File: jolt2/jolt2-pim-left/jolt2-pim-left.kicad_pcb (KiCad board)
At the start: 2 copper layers, 151 x 98 mm, 63 parts, among them J1 Conn_01x02_Pin, J10 Conn_01x02_Pin, J11 Conn_01x02_Pin, J12 Conn_01x02_Pin, J13 Conn_01x02_Pin, J14 Conn_01x02_Pin, J15 Conn_01x02_Pin, J16 Conn_01x02_Pin, J17 Conn_01x02_Pin, J18 Conn_01x02_Pin, J19 Conn_01x02_Pin, J2 Conn_01x02_Pin, J20 Conn_01x02_Pin, J21 Conn_01x02_Pin, J22 Conn_01x02_Pin, J23 Conn_01x02_Pin, J24 Conn_01x02_Pin, J25 Conn_01x02_Pin, J26 Conn_01x02_Pin, J27 Conn_01x02_Pin, J28 Conn_01x02_Pin, J29 USB_C_Receptacle_USB2.0_14P, J3 Conn_01x02_Pin, J30 Conn_ARM_JTAG_SWD_10, J31 RJ45, J4 Conn_01x02_Pin, J5 Conn_01x02_Pin, J6 Conn_01x02_Pin, J7 Conn_01x02_Pin, J8 Conn_01x02_Pin, J9 Conn_01x02_Pin, SW1 SW_SPST, SW2 SW_SPST, U1 RP2040, U3 W25Q128JVP, Y1 ABM8-272-T3

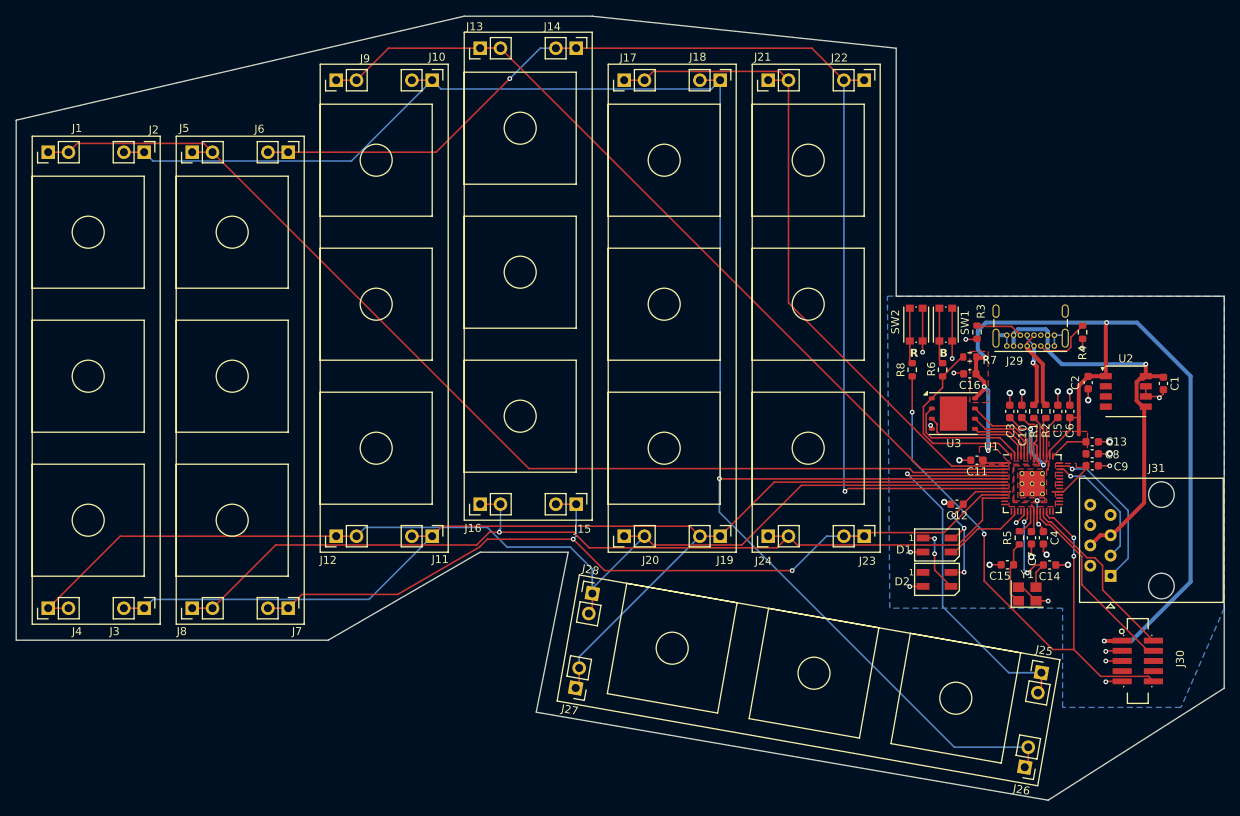
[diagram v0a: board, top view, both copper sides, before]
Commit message: jolt2-pim-left: Finalize routing
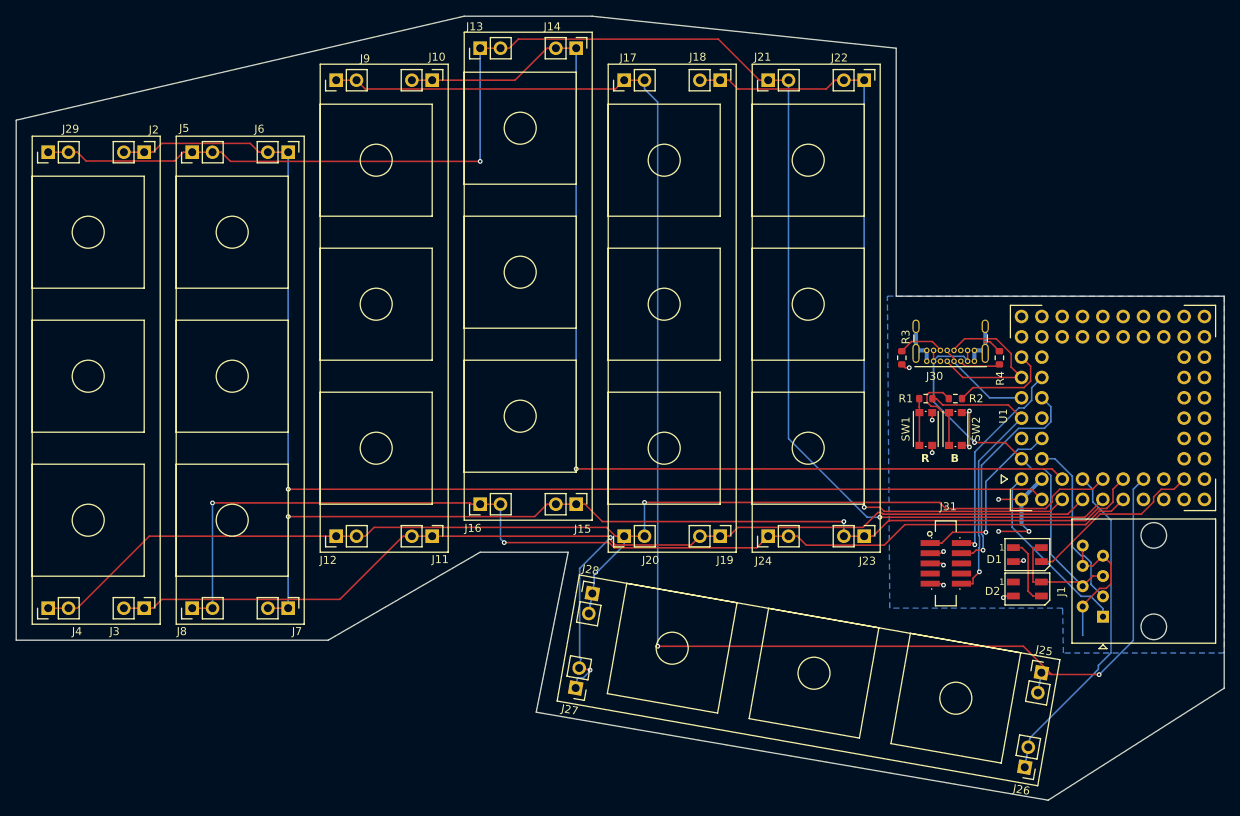
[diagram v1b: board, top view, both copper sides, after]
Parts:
- removed C1, C2: 10u, Capacitor_SMD:C_0603_1608Metric
- removed C10, C11, C12, C13, C3, C4, C7, C8, C9: 100n, Capacitor_SMD:C_0603_1608Metric
- removed C14, C15, C5, C6: 1u, Capacitor_SMD:C_0603_1608Metric
- removed C16: C, Capacitor_SMD:C_0603_1608Metric
- removed R5, R6, R8: 1k, Resistor_SMD:R_0603_1608Metric
- removed R7: 10k, Resistor_SMD:R_0603_1608Metric
- removed U2: ~, davidb-keyboard-foot:AP2112M-SO8
- removed U3: W25Q128JVP, Package_SON:WSON-8-1EP_6x5mm_P1.27mm_EP3.4x4.3mm
- removed Y1: ABM8-272-T3, Crystal:Crystal_SMD_Abracon_ABM8G-4Pin_3.2x2.5mm
- J1: value Conn_01x02_Pin -> RJ45; footprint Connector_PinHeader_2.54mm:PinHeader_1x02_P2.54mm_Vertical -> Connector_RJ:RJ45_Amphenol_54602-x08_Horizontal
- J29: value USB_C_Receptacle_USB2.0_14P -> Conn_01x02_Pin; footprint davidb-keyboard-foot:USB_C_Receptacle_GCT_USB4085 -> Connector_PinHeader_2.54mm:PinHeader_1x02_P2.54mm_Vertical
- J30: value Conn_ARM_JTAG_SWD_10 -> USB_C_Receptacle_USB2.0_14P; footprint davidb-keyboard-foot:Cortex-M-Debug10 -> davidb-keyboard-foot:USB_C_Receptacle_GCT_USB4085
- J31: value RJ45 -> Conn_ARM_JTAG_SWD_10; footprint Connector_RJ:RJ45_Amphenol_54602-x08_Horizontal -> davidb-keyboard-foot:Cortex-M-Debug10
- R1, R2: value 27 -> 1k
- R3, R4: value R -> 5.1k
- U1: value RP2040 -> ~; footprint davidb-keyboard-foot:RP2040-QFN-56 -> davidb-keyboard-foot:PIMORONI-PGA2035-PM722
- moved J1 144.1 mm to (172.8, 143.1)
- moved J29 128.1 mm to (41.0, 85.0), turned to 90 degrees
- moved J30 42.7 mm to (156.8, 111.1), turned to 180 degrees
- moved J31 20.7 mm to (153.2, 136.4), turned to 0 degrees
- moved SW2 13.9 mm to (154.4, 119.6)
- moved U1 13.8 mm to (174.1, 117.0), turned to 90 degrees
- moved R1 13.6 mm to (150.7, 115.8), turned to 180 degrees
- moved SW1 13.3 mm to (150.7, 119.6)
- moved R2 11.4 mm to (154.4, 115.8), turned to 0 degrees
- moved D1 11.4 mm to (163.4, 135.3)
- moved D2 11.4 mm to (163.4, 139.6)
- moved R4 10.9 mm to (159.9, 110.7), turned to 90 degrees
- moved R3 9.93 mm to (147.7, 110.7)
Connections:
- D1 pad 4: +3.3V -> VBUS
- D2 pad 4: +3.3V -> VBUS
- J1 pad 1: /COL-A -> SERRX
- J1 pad 2: /COL-A -> GND
- J10 pad 1: /ROW-A -> /COL-B
- J10 pad 2: /ROW-A -> /COL-B
- J11 pad 1: /ROW-B -> /ROW-A
- J11 pad 2: /ROW-B -> /ROW-A
- J12 pad 1: /ROW-C -> /ROW-B
- J12 pad 2: /ROW-C -> /ROW-B
- J13 pad 1: /COL-B -> /ROW-C
- J13 pad 2: /COL-B -> /ROW-C
- J14 pad 1: /ROW-D -> /COL-B
- J14 pad 2: /ROW-D -> /COL-B
- J15 pad 1: /ROW-E -> /ROW-D
- J15 pad 2: /ROW-E -> /ROW-D
- J16 pad 1: /ROW-F -> /ROW-E
- J16 pad 2: /ROW-F -> /ROW-E
- J17 pad 1: /COL-C -> /ROW-F
- J17 pad 2: /COL-C -> /ROW-F
- J18 pad 1: /ROW-A -> /COL-C
- J18 pad 2: /ROW-A -> /COL-C
- J19 pad 1: /ROW-B -> /ROW-A
- J19 pad 2: /ROW-B -> /ROW-A
- J2 pad 1: /ROW-A -> /COL-A
- J2 pad 2: /ROW-A -> /COL-A
- J20 pad 1: /ROW-C -> /ROW-B
- J20 pad 2: /ROW-C -> /ROW-B
- J21 pad 1: /COL-C -> /ROW-C
- J21 pad 2: /COL-C -> /ROW-C
- J22 pad 1: /ROW-D -> /COL-C
- J22 pad 2: /ROW-D -> /COL-C
- J23 pad 1: /ROW-E -> /ROW-D
- J23 pad 2: /ROW-E -> /ROW-D
- J24 pad 1: /ROW-F -> /ROW-E
- J24 pad 2: /ROW-F -> /ROW-E
- J25 pad 1: /COL-D -> /ROW-F
- J25 pad 2: /COL-D -> /ROW-F
- J26 pad 1: /ROW-A -> /COL-D
- J26 pad 2: /ROW-A -> /COL-D
- J27 pad 1: /ROW-B -> /ROW-A
- J27 pad 2: /ROW-B -> /ROW-A
- J28 pad 1: /ROW-C -> /ROW-B
- J28 pad 2: /ROW-C -> /ROW-B
- J3 pad 1: /ROW-B -> /ROW-A
- J3 pad 2: /ROW-B -> /ROW-A
- J31 pad 1: SERRX -> +3.3V
- J31 pad 2: GND -> SWDIO
- J31 pad 3: SERTX -> GND
- J31 pad 4: VBUS -> SWCLK
- J31 pad 5: VBUS -> GND
- J31 pad 6: GND -> unconnected-(J31-SWO/TDO-Pad6)
- J31 pad 7: GND -> unconnected-(J31-KEY-Pad7)
- J31 pad 8: GND -> unconnected-(J31-NC/TDI-Pad8)
- J4 pad 1: /ROW-C -> /ROW-B
- J4 pad 2: /ROW-C -> /ROW-B
- J5 pad 1: /COL-A -> /ROW-C
- J5 pad 2: /COL-A -> /ROW-C
- J6 pad 1: /ROW-D -> /COL-A
- J6 pad 2: /ROW-D -> /COL-A
- J7 pad 1: /ROW-E -> /ROW-D
- J7 pad 2: /ROW-E -> /ROW-D
- J8 pad 1: /ROW-F -> /ROW-E
- J8 pad 2: /ROW-F -> /ROW-E
- J9 pad 1: /COL-B -> /ROW-F
- J9 pad 2: /COL-B -> /ROW-F
- R1 pad 1: Net-(U1-USB_DP) -> RUN
- R1 pad 2: /USB_D+ -> Net-(SW1-B)
- R2 pad 1: Net-(U1-USB_DM) -> Net-(SW2-B)
- R2 pad 2: /USB_D- -> /BOOTSEL
- R3 pad 1: Net-(J29-CC2) -> Net-(J30-CC2)
- R4 pad 1: Net-(J29-CC1) -> Net-(J30-CC1)
- U1 pad 1: +3.3V -> SERRX
- U1 pad 10: +3.3V -> /ROW-E
- U1 pad 11: /ROW-E -> /ROW-F
- U1 pad 12: /ROW-F -> unconnected-(U1-GP12-Pad12)
- U1 pad 15: unconnected-(U1-GPIO12-Pad15) -> RGB
- U1 pad 16: RGB -> unconnected-(U1-GP16-Pad16)
- U1 pad 19: GND -> unconnected-(U1-GP19-Pad19)
- U1 pad 2: /COL-C -> /COL-A
- U1 pad 20: Net-(U1-XIN) -> unconnected-(U1-GP20-Pad20)
- U1 pad 21: Net-(U1-XOUT) -> unconnected-(U1-GP21-Pad21)
- U1 pad 22: +3.3V -> unconnected-(U1-GP22-Pad22)
- U1 pad 23: +1V1 -> unconnected-(U1-GP23-Pad23)
- U1 pad 24: SWCLK -> unconnected-(U1-GP24-Pad24)
- U1 pad 25: SWDIO -> unconnected-(U1-GP25-Pad25)
- U1 pad 26: RUN -> unconnected-(U1-GP26-Pad26)
- U1 pad 33: +3.3V -> unconnected-(U1-GP33-Pad33)
- U1 pad 4: /COL-A -> /COL-C
- U1 pad 40: SERTX -> unconnected-(U1-GP40-Pad40)
- U1 pad 41: SERRX -> unconnected-(U1-GP41-Pad41)
- U1 pad 42: +3.3V -> unconnected-(U1-GP42-Pad42)
- U1 pad 43: +3.3V -> unconnected-(U1-GP43-Pad43)
- U1 pad 44: +3.3V -> unconnected-(U1-GP44-Pad44)
- U1 pad 45: +1V1 -> unconnected-(U1-GP45-Pad45)
- U1 pad 46: Net-(U1-USB_DM) -> unconnected-(U1-GP46-Pad46)
- U1 pad 47: Net-(U1-USB_DP) -> unconnected-(U1-GP47-Pad47)
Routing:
- net +3.3V: track 162.2 -> 23.1 mm, vias 8 -> 1
- net /ROW-A: track 228.4 -> 149.5 mm, vias 1 -> 2
- net /ROW-F: track 120.1 -> 198.1 mm, vias 1 -> 2
- net /ROW-C: track 143.6 -> 199.8 mm, vias 0 -> 2
- net RUN: track 74.7 -> 37.0 mm, vias 4 -> 1
- net /ROW-E: track 110.0 -> 137.8 mm
- net /ROW-D: track 153.2 -> 125.6 mm
- net /COL-B: track 109.6 -> 136.1 mm, vias 0 -> 1
- net +1V1: track 24.3 -> 0.00 mm, vias 4 -> 0
- net QSPI.SS: track 23.9 -> 0.00 mm
- net /COL-A: track 139.6 -> 158.3 mm, vias 0 -> 1
- net QSPI.SD1: track 15.8 -> 0.00 mm
- net QSPI.SD2: track 14.1 -> 0.00 mm
- net Net-(U1-XIN): track 13.6 -> 0.00 mm, vias 2 -> 0
- net /COL-C: track 87.3 -> 100.4 mm, vias 0 -> 1
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- removed copper zone on F.Cu, net +1V1
- removed copper zone on F.Cu, net +3.3V

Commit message: jolt2-pim-left: Add uart terminating resistors
Place 27 ohm series resisters on the inter-board uart lines.
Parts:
- added R5: 27, Resistor_SMD:R_0603_1608Metric_Pad0.98x0.95mm_HandSolder, F.Cu at (164.5, 143.2)
- added R6: 27, Resistor_SMD:R_0603_1608Metric_Pad0.98x0.95mm_HandSolder, F.Cu at (164.5, 144.7)
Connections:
- U1 pad 0: SERTX -> Net-(U1-GP0)
- U1 pad 1: SERRX -> Net-(U1-GP1)
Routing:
- net Net-(U1-GP0): track 0.00 -> 27.1 mm, vias 0 -> 3
- net Net-(U1-GP1): track 0.00 -> 22.2 mm, vias 0 -> 1
- net SERRX: track 23.1 -> 8.12 mm
- net SERTX: track 21.5 -> 8.63 mm
